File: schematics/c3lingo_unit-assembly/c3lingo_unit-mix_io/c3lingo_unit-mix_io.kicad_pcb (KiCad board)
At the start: 2 copper layers, 100 x 50 mm, 40 parts, among them J201 Stage Line-In, J202 Mix Line-Out, J203 PowerSupply, J204 Inputs, J205 Output, U201 LM833N, U202 DRV134PA, U203 LM833N

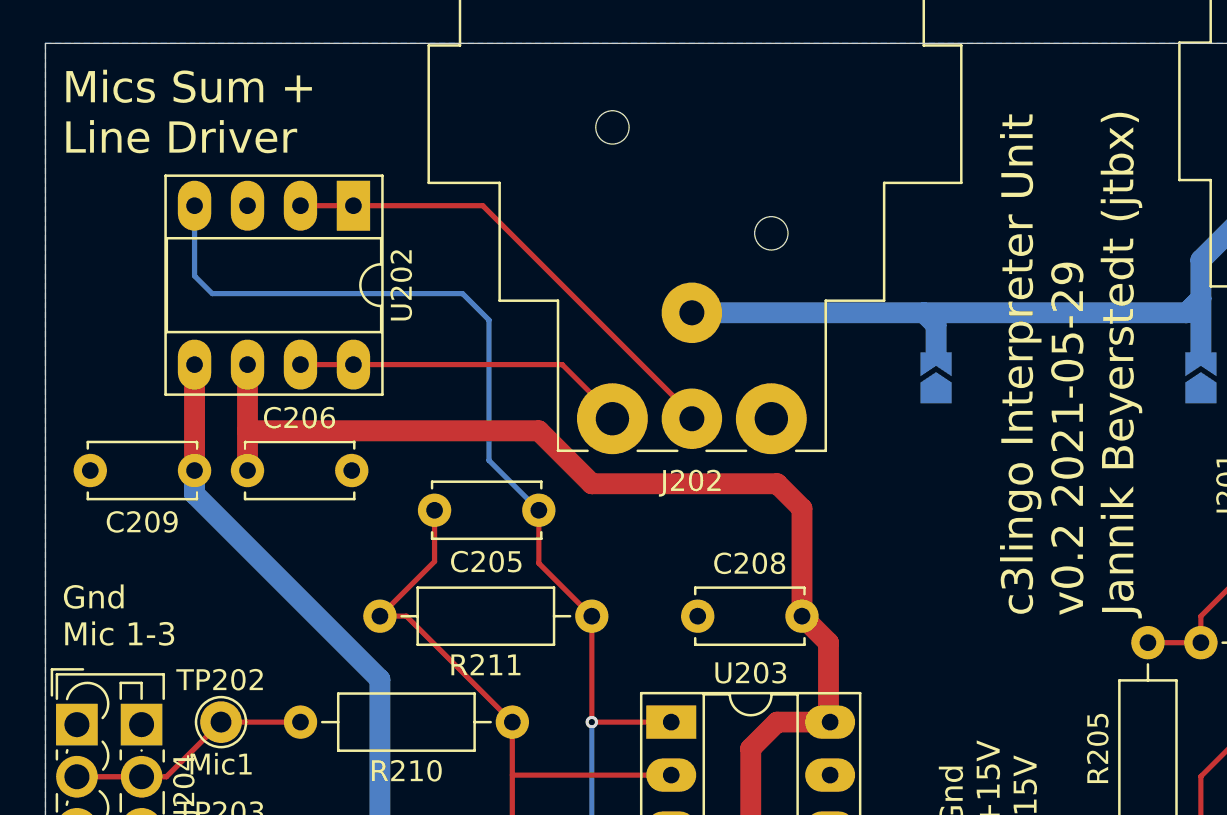
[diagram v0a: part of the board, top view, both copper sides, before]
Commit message: PCB: Update for new schematic (still THT for now)
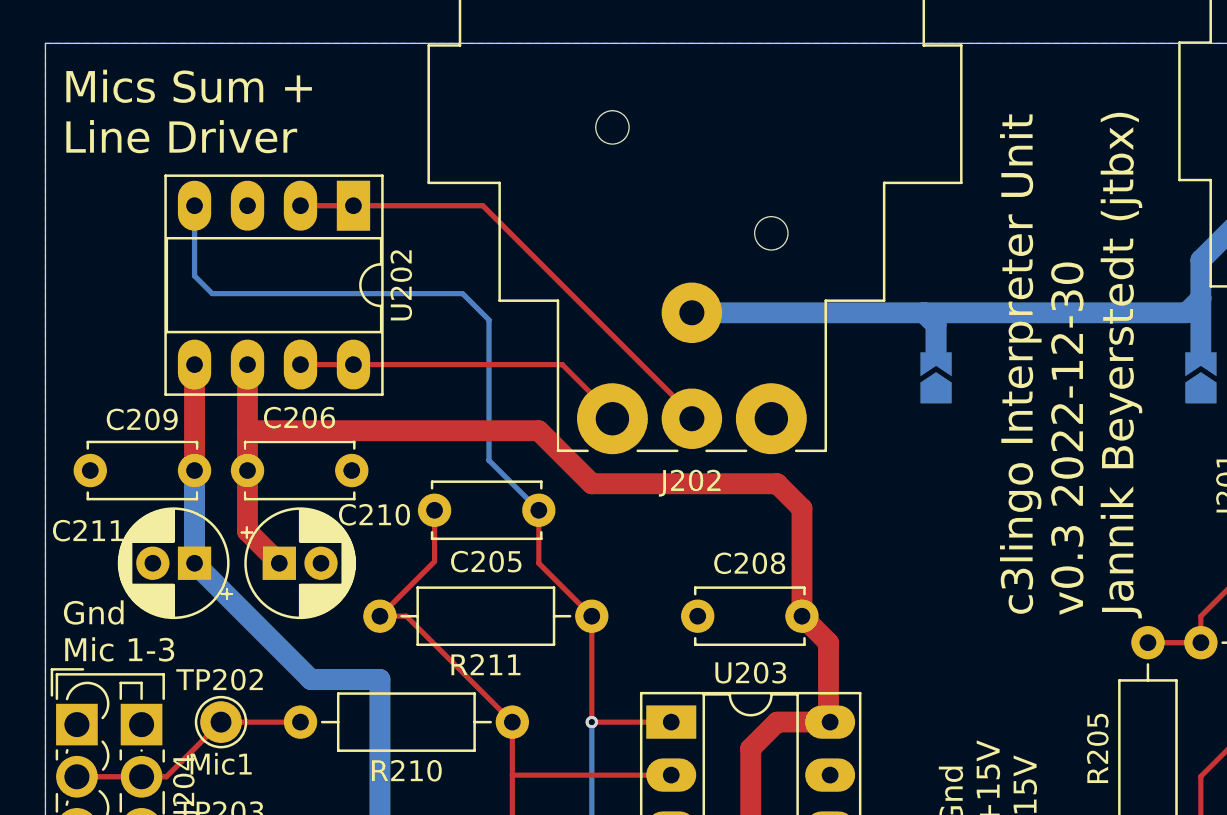
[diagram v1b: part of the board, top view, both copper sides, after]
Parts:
- added C210: 10uF, Capacitor_THT:CP_Radial_D5.0mm_P2.00mm, F.Cu at (61.2, 74.9)
- added C211: 10uF, Capacitor_THT:CP_Radial_D5.0mm_P2.00mm, F.Cu at (57.1, 74.9)
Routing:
- net +15V: track 153.9 -> 159.0 mm
- net -15V: track 135.6 -> 137.6 mm
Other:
- board text added: "c3lingo Interpreter Unit v0.3 2022-12-30 Jannik Beyerstedt (jtbx)"
- board text removed: "c3lingo Interpreter Unit v0.2 2021-05-29 Jannik Beyerstedt (jtbx)"

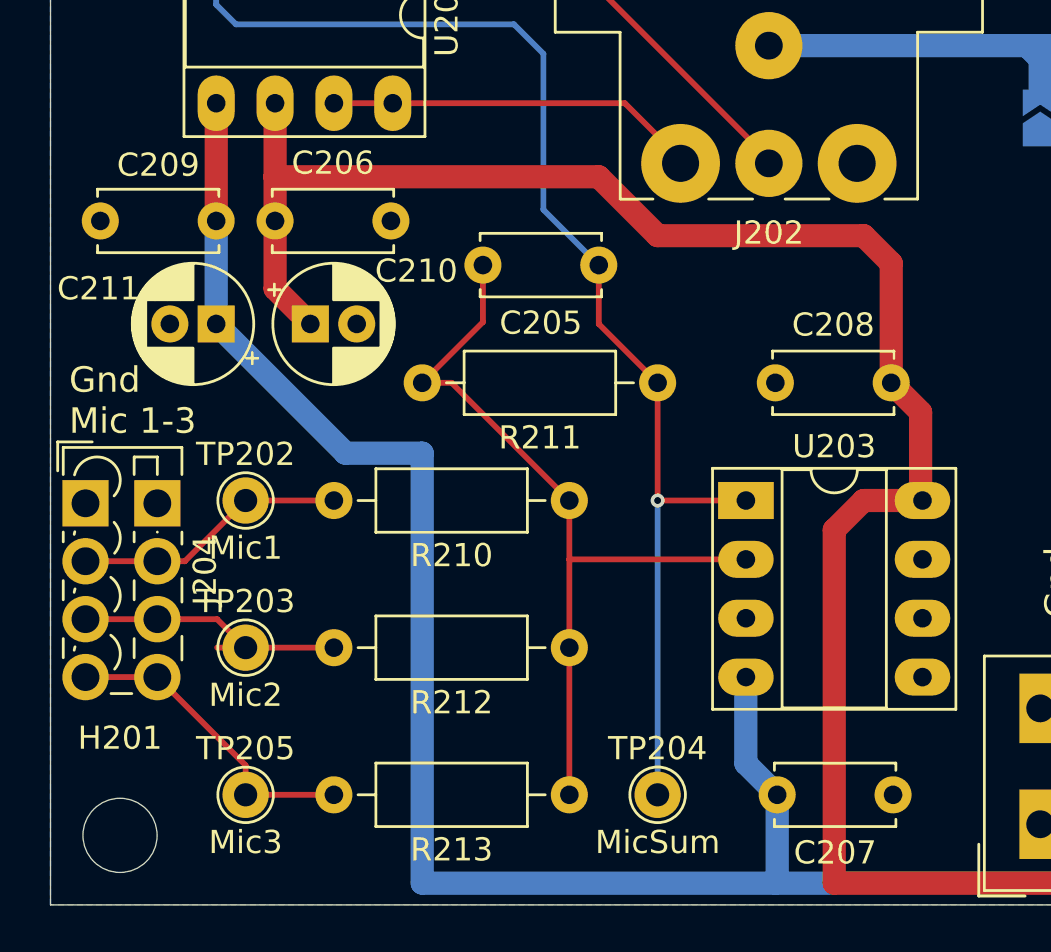
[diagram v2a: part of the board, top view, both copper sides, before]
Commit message: [TIDY] Split channel into two schematics
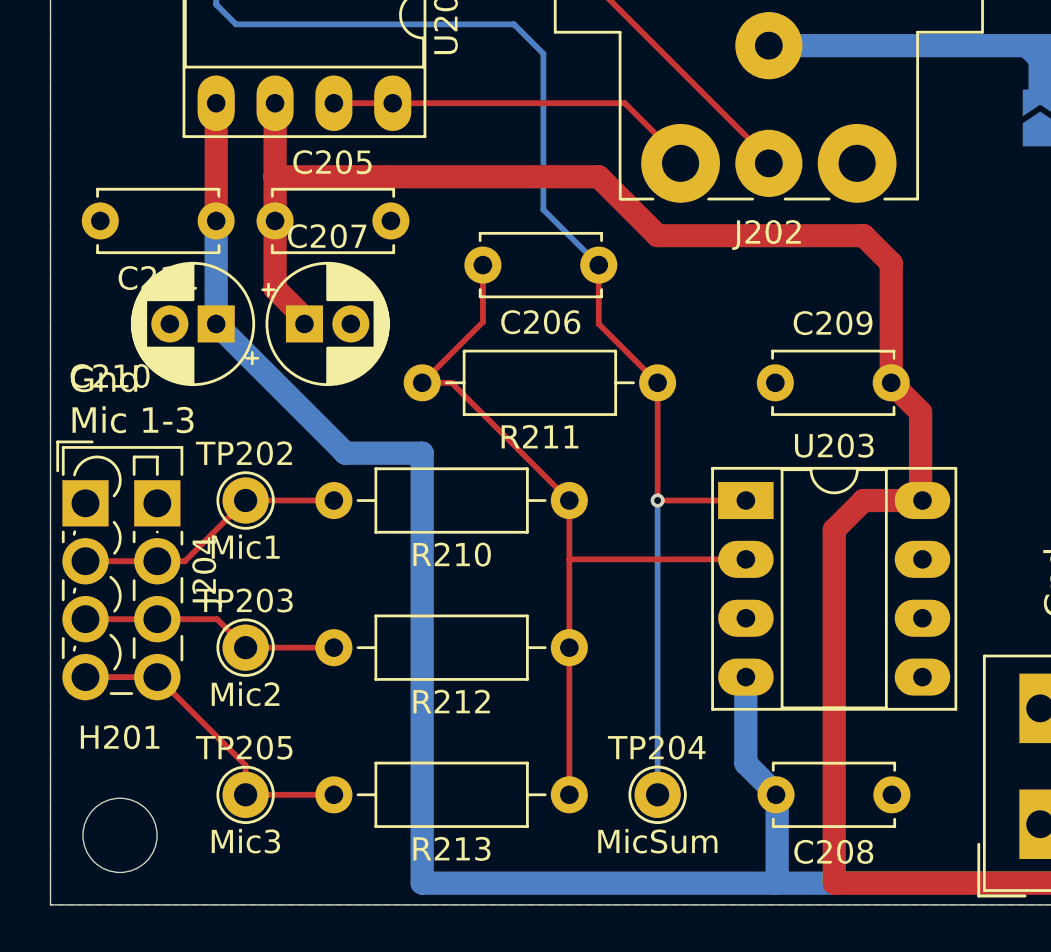
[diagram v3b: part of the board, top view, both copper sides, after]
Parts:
- C205: value 22pF -> 100nF
- C206: value 100nF -> 22pF
- C207: value 100nF -> 10uF; footprint Capacitor_THT:C_Disc_D5.0mm_W2.5mm_P5.00mm -> Capacitor_THT:CP_Radial_D5.0mm_P2.00mm
- C211: value 10uF -> 100nF; footprint Capacitor_THT:CP_Radial_D5.0mm_P2.00mm -> Capacitor_THT:C_Disc_D5.0mm_W2.5mm_P5.00mm
- moved C207 32.5 mm to (61.0, 74.9), turned to 0 degrees
- moved C209 25.1 mm to (81.3, 77.5), turned to 0 degrees
- moved C208 18.5 mm to (86.3, 95.2), turned to 180 degrees
- moved C205 14.1 mm to (59.7, 70.5), turned to 0 degrees
- moved C206 14.1 mm to (73.7, 72.4), turned to 180 degrees
- moved C211 4.45 mm to (57.1, 70.5)
- moved C210 4.06 mm to (57.1, 74.9), turned to 180 degrees
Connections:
- C205 pad 1: Net-(C205-Pad1) -> +15V
- C205 pad 2: Net-(C205-Pad2) -> GND
- C206 pad 1: +15V -> Net-(C206-Pad1)
- C206 pad 2: GND -> Net-(C206-Pad2)
- C207 pad 1: GND -> +15V
- C207 pad 2: -15V -> GND
- C208 pad 2: +15V -> -15V
- C209 pad 1: -15V -> GND
- C209 pad 2: GND -> +15V
- C210 pad 1: +15V -> -15V
- R210 pad 1: Net-(C205-Pad2) -> Net-(C206-Pad2)
- R211 pad 1: Net-(C205-Pad1) -> Net-(C206-Pad1)
- R211 pad 2: Net-(C205-Pad2) -> Net-(C206-Pad2)
- R212 pad 1: Net-(C205-Pad2) -> Net-(C206-Pad2)
- R213 pad 1: Net-(C205-Pad2) -> Net-(C206-Pad2)
- TP204 pad 1: Net-(C205-Pad1) -> Net-(C206-Pad1)
- U202 pad 4: Net-(C205-Pad1) -> Net-(C206-Pad1)
- U203 pad 1: Net-(C205-Pad1) -> Net-(C206-Pad1)
- U203 pad 2: Net-(C205-Pad2) -> Net-(C206-Pad2)
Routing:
- net Net-(C206-Pad1): track 0.00 -> 56.2 mm, vias 0 -> 1
- net Net-(C205-Pad1): track 56.2 -> 0.00 mm, vias 1 -> 0
- net Net-(C206-Pad2): track 0.00 -> 34.9 mm
- net Net-(C205-Pad2): track 34.9 -> 0.00 mm
- net /Mix_Ch2: track 12.5 -> 11.2 mm

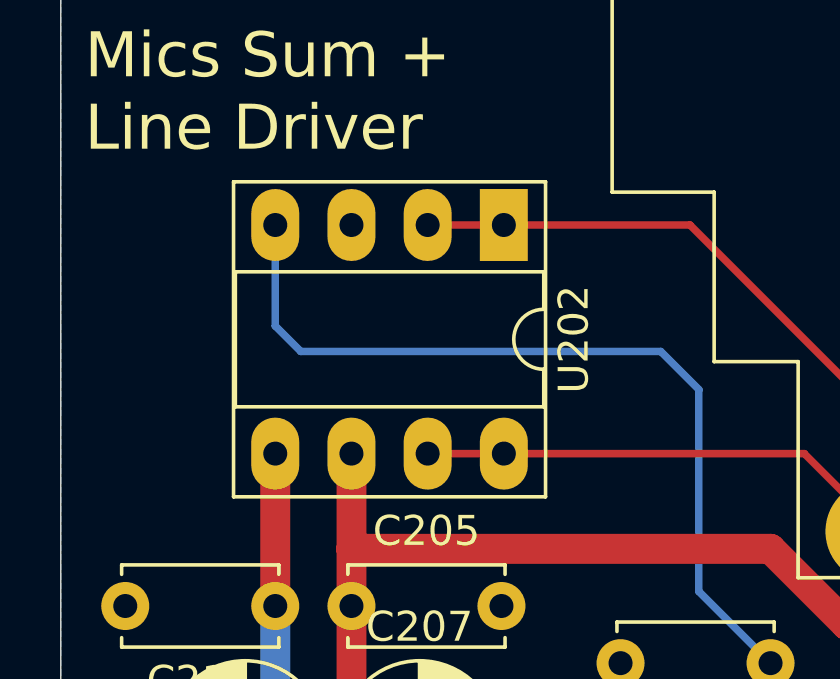
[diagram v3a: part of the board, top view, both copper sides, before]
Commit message: Update to KiCad 7
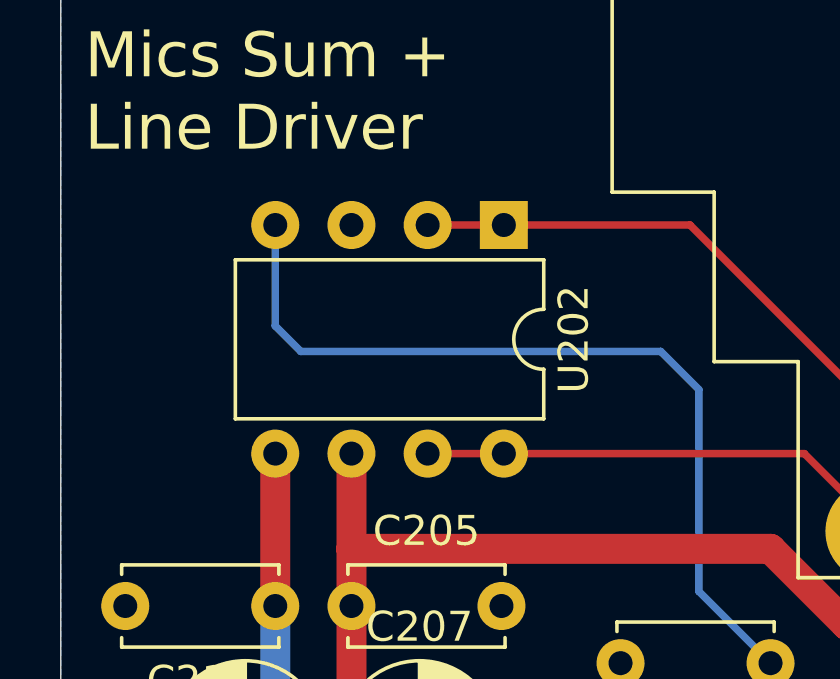
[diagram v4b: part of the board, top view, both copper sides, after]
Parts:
- U202: footprint Package_DIP:DIP-8_W7.62mm_Socket_LongPads -> Package_DIP:DIP-8_W7.62mm

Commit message: Reworks board-to-board connections
Instead of having connections between all boards, use the mix_io board as an audio signal distribution hub.

Note: PCB not updated
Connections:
- net /Mix_Ch1 renamed /Mic_Ch1
- net /Mix_Ch2 renamed /Mic_Ch2
- net /Mix_Ch3 renamed /Mic_Ch3
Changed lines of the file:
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@@
   (net 10 "Net-(J201-Pad2)")
   (net 11 "GNDREF")
-  (net 12 "/Mix_Ch3")
-  (net 13 "/Mix_Ch2")
-  (net 14 "/Mix_Ch1")
+  (net 12 "/Mic_Ch3")
+  (net 13 "/Mic_Ch2")
+  (net 14 "/Mic_Ch1")
   (net 15 "Net-(U203A--)")
   (net 16 "Net-(R201-Pad1)")
@@
       (net 15 "Net-(U203A--)") (pintype "passive"))
     (pad "2" thru_hole oval (at 10.16 0 180) (size 1.6 1.6) (drill 0.8) (layers "*.Cu" "*.Mask")
-      (net 14 "/Mix_Ch1") (pintype "passive"))
+      (net 14 "/Mic_Ch1") (pintype "passive"))
     (model "${KICAD6_3DMODEL_DIR}/Resistor_THT.3dshapes/R_Axial_DIN0207_L6.3mm_D2.5mm_P10.16mm_Horizontal.wrl"
       (offset (xyz 0 0 0))
@@
       (net 15 "Net-(U203A--)") (pintype "passive"))
     (pad "2" thru_hole oval (at 10.16 0 180) (size 1.6 1.6) (drill 0.8) (layers "*.Cu" "*.Mask")
-      (net 13 "/Mix_Ch2") (pintype "passive"))
+      (net 13 "/Mic_Ch2") (pintype "passive"))
     (model "${KICAD6_3DMODEL_DIR}/Resistor_THT.3dshapes/R_Axial_DIN0207_L6.3mm_D2.5mm_P10.16mm_Horizontal.wrl"
       (offset (xyz 0 0 0))
@@
       (net 15 "Net-(U203A--)") (pintype "passive"))
     (pad "2" thru_hole oval (at 10.16 0 180) (size 1.6 1.6) (drill 0.8) (layers "*.Cu" "*.Mask")
-      (net 12 "/Mix_Ch3") (pintype "passive"))
+      (net 12 "/Mic_Ch3") (pintype "passive"))
     (model "${KICAD6_3DMODEL_DIR}/Resistor_THT.3dshapes/R_Axial_DIN0207_L6.3mm_D2.5mm_P10.16mm_Horizontal.wrl"
       (offset (xyz 0 0 0))
@@
       (stroke (width 0.05) (type solid)) (fill none) (layer "F.CrtYd"))
     (pad "1" thru_hole circle (at 0 0) (size 2 2) (drill 1) (layers "*.Cu" "*.Mask")
-      (net 14 "/Mix_Ch1") (pinfunction "1") (pintype "passive"))
+      (net 14 "/Mic_Ch1") (pinfunction "1") (pintype "passive"))
   )
   (footprint "TestPoint:TestPoint_THTPad_D2.0mm_Drill1.0mm" (layer "F.Cu")
@@
       (stroke (width 0.05) (type solid)) (fill none) (layer "F.CrtYd"))
     (pad "1" thru_hole circle (at 0 0) (size 2 2) (drill 1) (layers "*.Cu" "*.Mask")
-      (net 13 "/Mix_Ch2") (pinfunction "1") (pintype "passive"))
+      (net 13 "/Mic_Ch2") (pinfunction "1") (pintype "passive"))
   )
   (footprint "TestPoint:TestPoint_THTPad_D2.0mm_Drill1.0mm" (layer "F.Cu")
@@
       (stroke (width 0.05) (type solid)) (fill none) (layer "F.CrtYd"))
     (pad "1" thru_hole circle (at 0 0) (size 2 2) (drill 1) (layers "*.Cu" "*.Mask")
-      (net 12 "/Mix_Ch3") (pinfunction "1") (pintype "passive"))
+      (net 12 "/Mic_Ch3") (pinfunction "1") (pintype "passive"))
   )
   (footprint "Capacitor_THT:C_Disc_D5.0mm_W2.5mm_P5.00mm" (layer "F.Cu")
@@
       (net 3 "GND") (pinfunction "Pin_1") (pintype "passive"))
     (pad "2" thru_hole circle (at 2.5 -3.1 270) (size 2 2) (drill 1.2) (layers "*.Cu" "*.Mask")
-      (net 14 "/Mix_Ch1") (pinfunction "Pin_2") (pintype "passive"))
+      (net 14 "/Mic_Ch1") (pinfunction "Pin_2") (pintype "passive"))
     (pad "2" thru_hole circle (at 2.5 0 270) (size 2 2) (drill 1.2) (layers "*.Cu" "*.Mask")
-      (net 14 "/Mix_Ch1") (pinfunction "Pin_2") (pintype "passive"))
+      (net 14 "/Mic_Ch1") (pinfunction "Pin_2") (pintype "passive"))
     (pad "3" thru_hole circle (at 5 -3.1 270) (size 2 2) (drill 1.2) (layers "*.Cu" "*.Mask")
-      (net 13 "/Mix_Ch2") (pinfunction "Pin_3") (pintype "passive"))
+      (net 13 "/Mic_Ch2") (pinfunction "Pin_3") (pintype "passive"))
     (pad "3" thru_hole circle (at 5 0 270) (size 2 2) (drill 1.2) (layers "*.Cu" "*.Mask")
-      (net 13 "/Mix_Ch2") (pinfunction "Pin_3") (pintype "passive"))
+      (net 13 "/Mic_Ch2") (pinfunction "Pin_3") (pintype "passive"))
     (pad "4" thru_hole circle (at 7.5 -3.1 270) (size 2 2) (drill 1.2) (layers "*.Cu" "*.Mask")
-      (net 12 "/Mix_Ch3") (pinfunction "Pin_4") (pintype "passive"))
+      (net 12 "/Mic_Ch3") (pinfunction "Pin_4") (pintype "passive"))
     (pad "4" thru_hole circle (at 7.5 0 270) (size 2 2) (drill 1.2) (layers "*.Cu" "*.Mask")
-      (net 12 "/Mix_Ch3") (pinfunction "Pin_4") (pintype "passive"))
+      (net 12 "/Mic_Ch3") (pinfunction "Pin_4") (pintype "passive"))
     (model "${KICAD6_3DMODEL_DIR}/TerminalBlock_Phoenix.3dshapes/TerminalBlock_Phoenix_PTSM-0,5-4-2.5-V-THR_1x04_P2.50mm_Vertical.wrl"
       (offset (xyz 0 0 0))
